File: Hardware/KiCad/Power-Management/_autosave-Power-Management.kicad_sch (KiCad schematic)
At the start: 31 parts, among them IC1 RT9080-33GJ5, J1 Screw_Terminal_01x02, J2 Conn_01x06, J3 Screw_Terminal_01x02, K1 FINDER-36.11, Q1 BC817, U1 STM32F401CCU6, U3 ESP-01, Y1 25Mhz

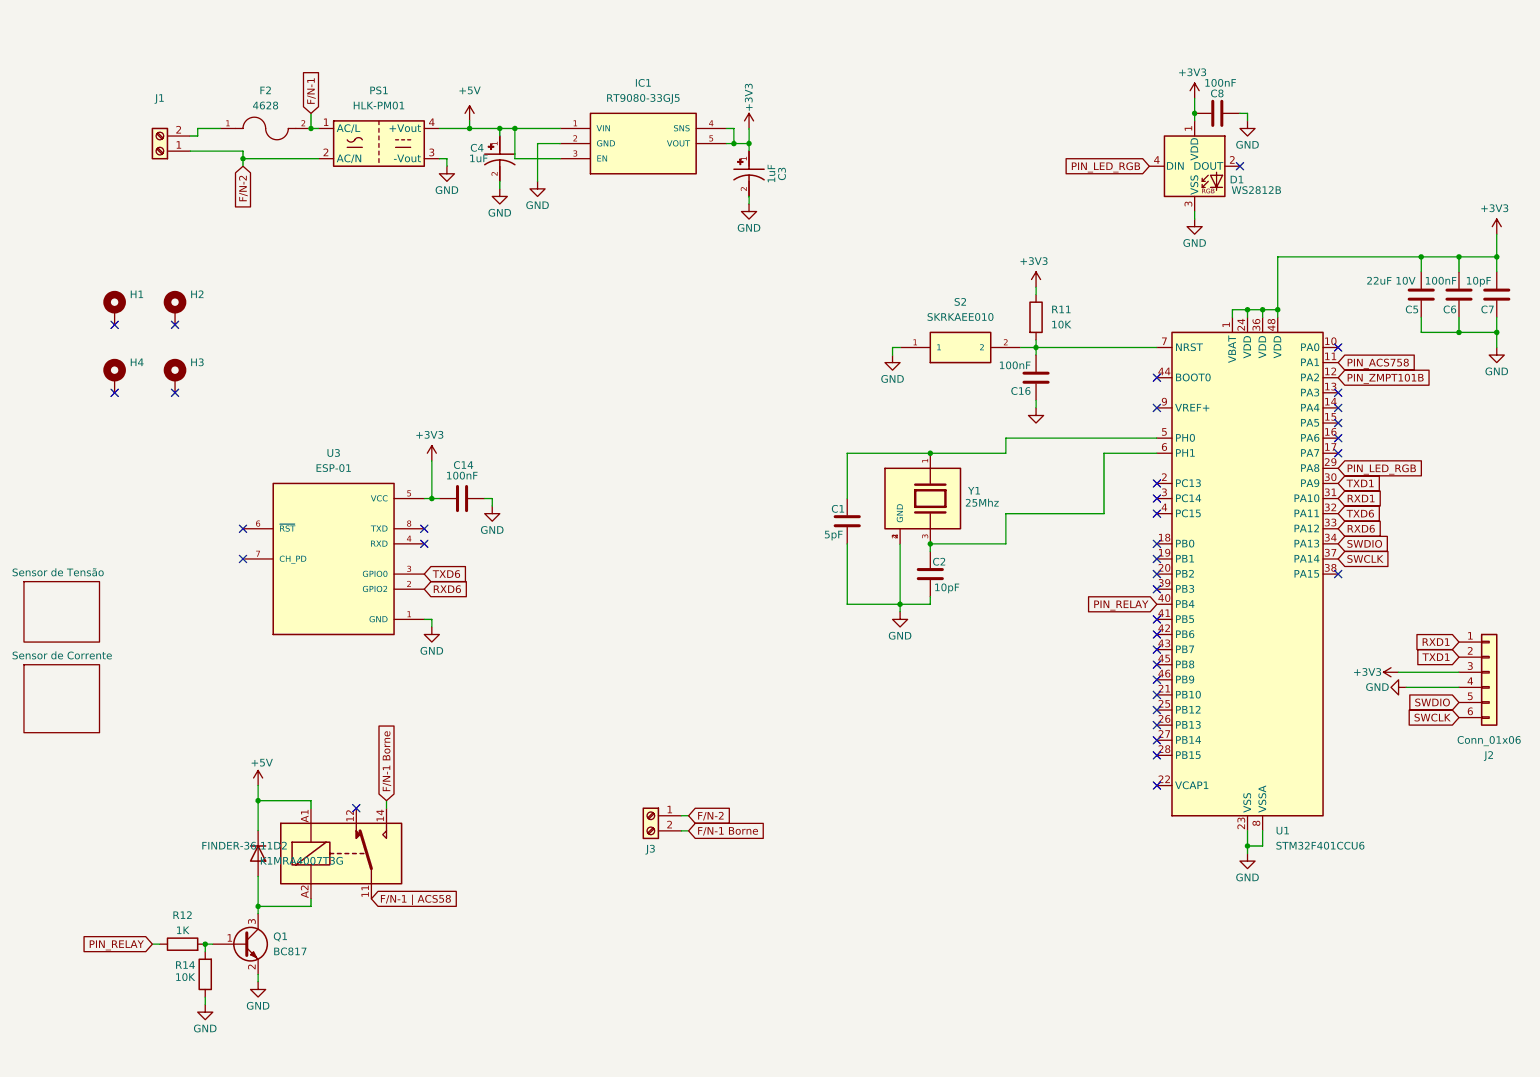
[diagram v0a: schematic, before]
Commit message: refactor: exchange of STMF401 for F103
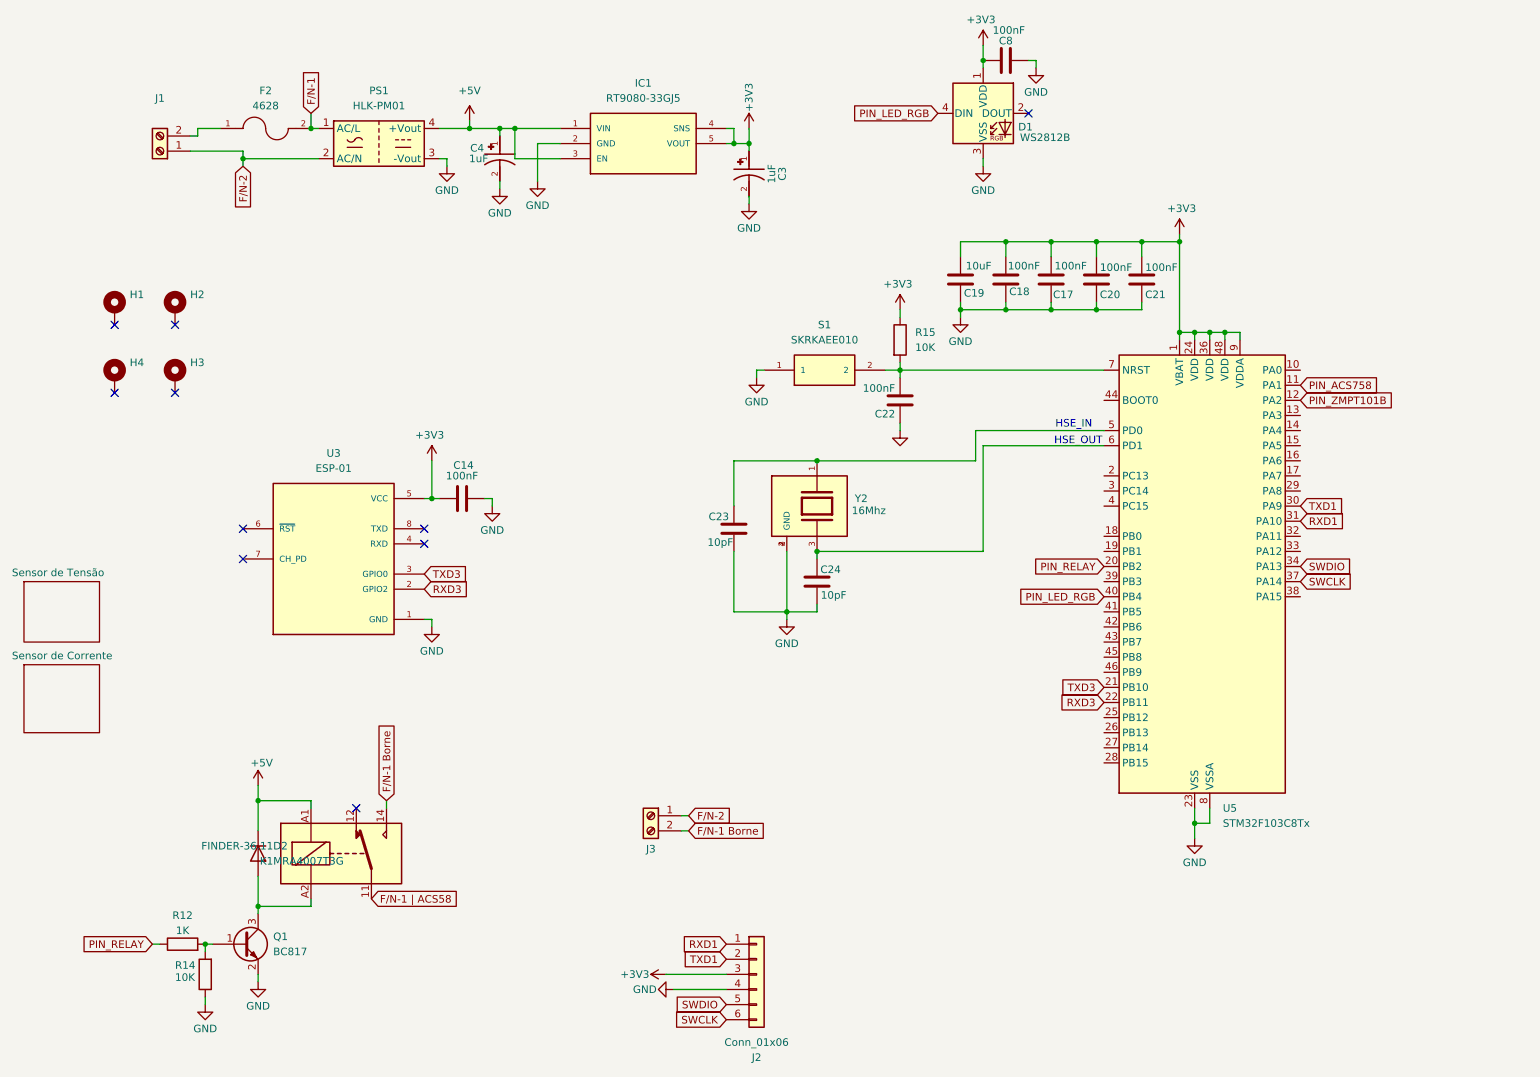
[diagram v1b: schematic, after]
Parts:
- removed C1: 5pF, Capacitor_SMD:C_0805_2012Metric, symbol Device:C
- removed C16, C6: 100nF, Capacitor_SMD:C_0805_2012Metric, symbol Device:C
- removed C2, C7: 10pF, Capacitor_SMD:C_0805_2012Metric, symbol Device:C
- removed C5: 22uF 10V, Capacitor_SMD:C_0805_2012Metric, symbol Device:C
- removed R11: 10K, Resistor_SMD:R_0805_2012Metric_Pad1.20x1.40mm_HandSolder, symbol Device:R
- removed S2: SKRKAEE010, SKRKAEE010:SKRK, symbol SKRKAEE010:SKRKAEE010
- removed U1: STM32F401CCU6, Package_DFN_QFN:QFN-48-1EP_7x7mm_P0.5mm_EP3.5x3.5mm, symbol MCU_ST_STM32F4:STM32F401CCUx
- removed Y1: 25Mhz, TSX-3225_25.0000MF10Z-W:XTAL_TSX-3225_25.0000MF10Z-W, symbol TSX-3225_25.0000MF10Z-W:TSX-3225_25.0000MF10Z-W
- added C17, C18, C20, C21, C22: 100nF, Capacitor_SMD:C_0805_2012Metric, symbol Device:C
- added C19: 10uF, Capacitor_SMD:C_0805_2012Metric, symbol Device:C
- added C23, C24: 10pF, Capacitor_SMD:C_0805_2012Metric, symbol Device:C
- added R15: 10K, Resistor_SMD:R_0805_2012Metric_Pad1.20x1.40mm_HandSolder, symbol Device:R
- added S1: SKRKAEE010, SKRKAEE010:SKRK, symbol SKRKAEE010:SKRKAEE010
- added U5: STM32F103C8Tx, Package_QFP:LQFP-48_7x7mm_P0.5mm, symbol MCU_ST_STM32F1:STM32F103C8Tx
- added Y2: 16Mhz, TSX-3225_25.0000MF10Z-W:XTAL_TSX-3225_25.0000MF10Z-W, symbol TSX-3225_25.0000MF10Z-W:TSX-3225_25.0000MF10Z-W
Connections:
- net +3V3: now also C17.2, C18.2, C19.2, C20.2, C21.2, R15.1, U5.1 (VBAT), U5.24 (VDD), U5.36 (VDD), U5.48 (VDD), U5.9 (VDDA)
- net GND: now also C17.1, C18.1, C19.1, C20.1, C21.1, C22.1, C23.1, C24.1, S1.1, U5.23 (VSS), U5.35 (VSS), U5.47 (VSS), U5.8 (VSSA), Y2.2 (GND), Y2.4 (GND)
- net PIN_ACS758: now also U5.11 (PA1)
- net PIN_LED_RGB: now also U5.40 (PB4)
- net PIN_RELAY: now also U5.20 (PB2)
- net PIN_ZMPT101B: now also U5.12 (PA2)
- net RXD1: now also U5.31 (PA10)
- net SWCLK: now also U5.37 (PA14)
- net SWDIO: now also U5.34 (PA13)
- net TXD1: now also U5.30 (PA9)
- net RXD6 renamed RXD3
- net RXD3: now also U5.22 (PB11)
- net TXD6 renamed TXD3
- net TXD3: now also U5.21 (PB10)
- new net: C22.2, R15.2, S1.2, U5.7 (NRST)
- new net: C23.2, U5.5 (PD0), Y2.1
- new net: C24.2, U5.6 (PD1), Y2.3
- no-connect marks 37 -> 10
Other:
- note added: "HSE_IN"
- note added: "HSE_OUT"
- moved on the sheet: C8, D1, J2
